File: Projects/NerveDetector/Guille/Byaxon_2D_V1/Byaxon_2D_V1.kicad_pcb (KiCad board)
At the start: 2 copper layers, 120.3 x 90 mm, 77 parts, among them U1 TL074

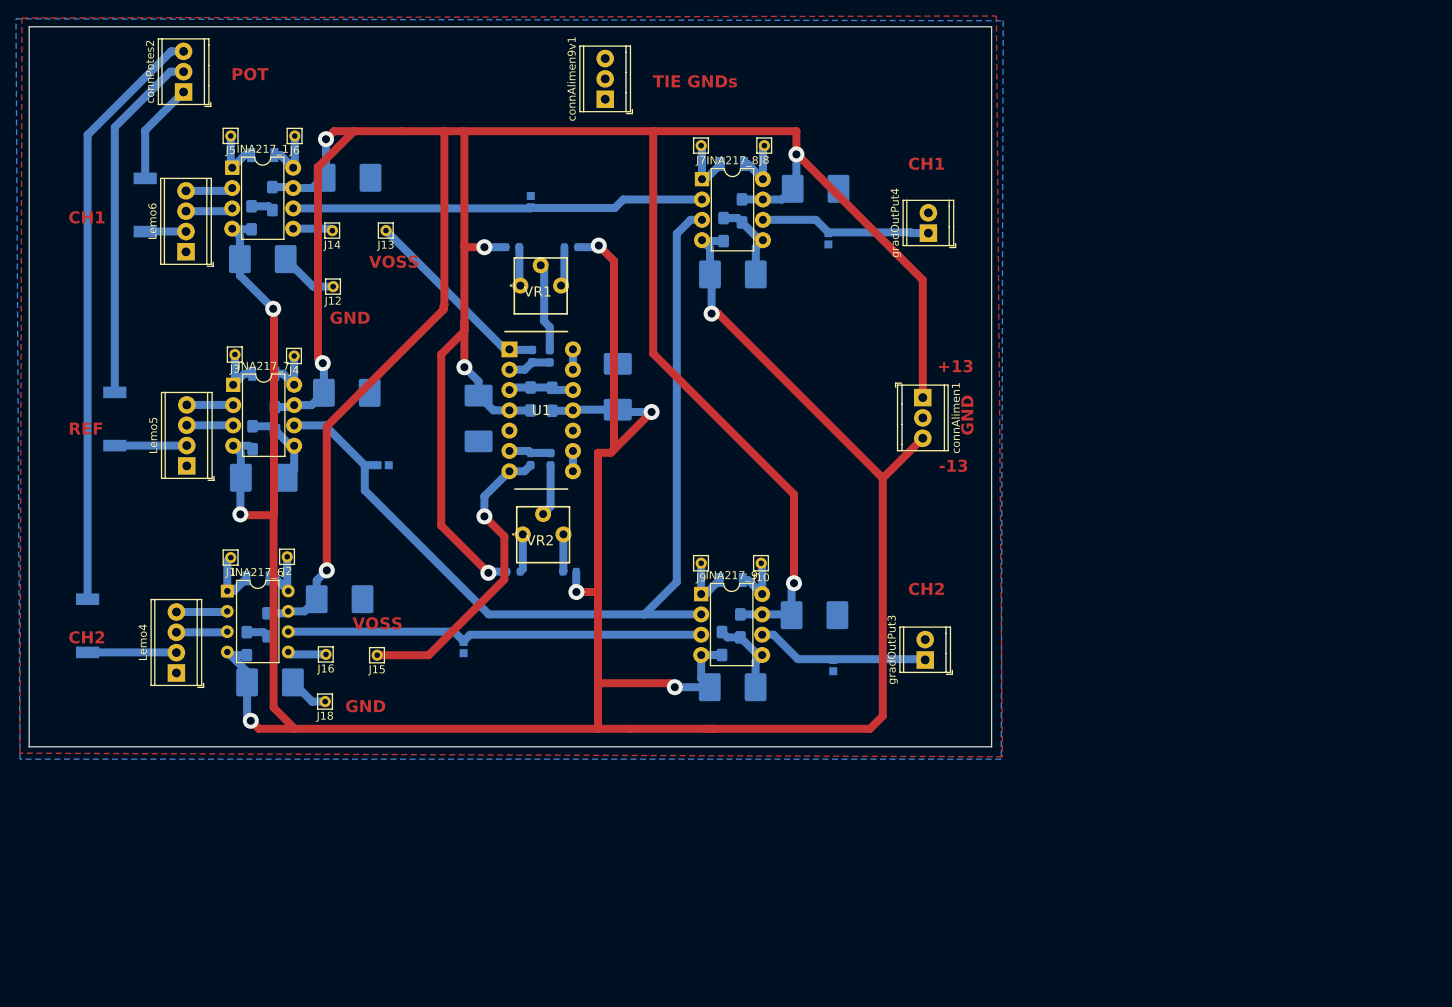
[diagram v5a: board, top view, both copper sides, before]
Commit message: Added link to projects github on the PCB
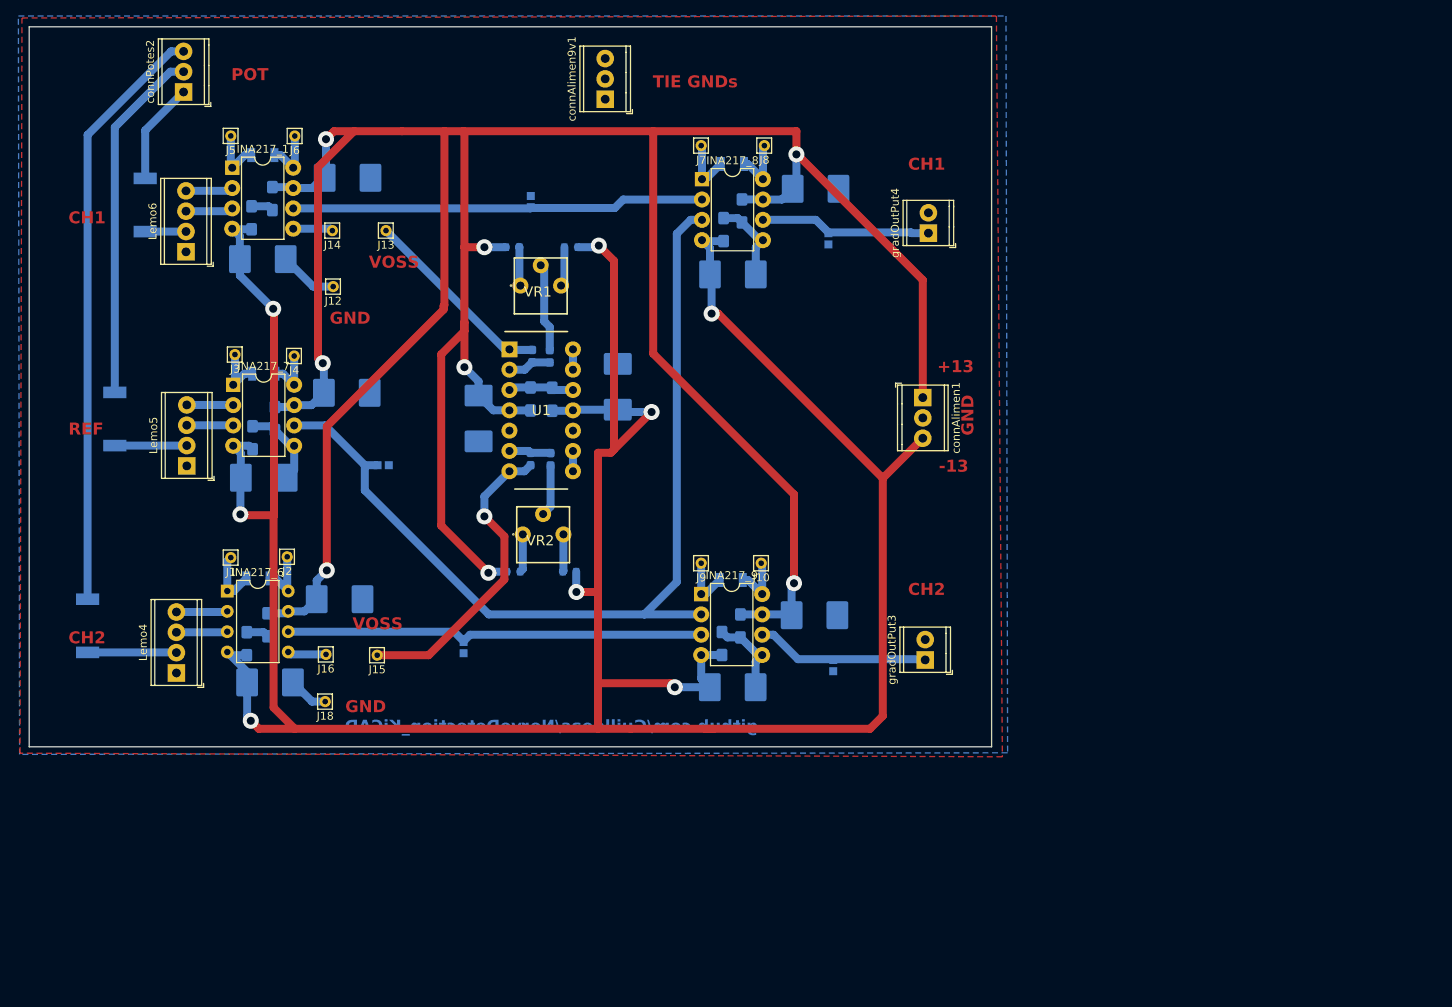
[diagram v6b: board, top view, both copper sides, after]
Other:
- board text added: "github.com/Guilldeas/NerveDetection_KiCAD"
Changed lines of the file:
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@@
     (effects (font (size 1.5 1.5) (thickness 0.3) bold) (justify left bottom))
+  )
+  (gr_text "github.com/Guilldeas/NerveDetection_KiCAD" (at 123.6 126.55) (layer "B.Cu")
+    (effects (font (size 1.5 1.5) (thickness 0.3) bold) (justify left bottom mirror))
   )
   (segment (start 112.7 120.3) (end 113.2 120.8) (width 1) (layer "F.Cu") (net 1))
@@
     (polygon
       (pts
-        (xy 30.85 37.25)
-        (xy 154.25 37.5)
-        (xy 154 129.8)
-        (xy 31.35 129.8)
+        (xy 154.6 36.9)
+        (xy 154.8 129)
+        (xy 31.3 129.2)
+        (xy 31.15 36.9)
       )
     )

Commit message: Added mounting holes
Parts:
- added H1: MountingHole, MountingHole:MountingHole_3.2mm_M3, F.Cu at (91.2, 72.0)
- added H2: MountingHole, MountingHole:MountingHole_3.2mm_M3, F.Cu at (90.5, 151.9)
- added H3: MountingHole, MountingHole:MountingHole_3.2mm_M3, F.Cu at (202.1, 152.9)
- added H4: MountingHole_Pad, MountingHole:MountingHole_3.2mm_M3_DIN965_Pad, F.Cu at (200.9, 72.0)
- moved C2 60.7 mm to (159.6, 112.0)
- moved C22 60.7 mm to (172.8, 92.3)
- moved R16 60.7 mm to (140.3, 144.6)
- moved R28 60.7 mm to (151.1, 108.2)
- moved VR2 60.7 mm to (150.2, 134.0)
- moved C39 60.7 mm to (116.4, 88.5)
- moved INA217_6 60.7 mm to (110.8, 137.5)
- moved Lemo4 60.7 mm to (104.4, 147.7)
- moved C1 60.7 mm to (142.2, 115.9)
- moved C21 60.7 mm to (174.0, 97.9)
- moved C23 60.7 mm to (116.7, 115.9)
- moved C24 60.7 mm to (125.7, 112.7)
- moved C25 60.7 mm to (184.2, 140.5)
- moved C27 60.7 mm to (175.1, 90.0)
- moved C28 60.7 mm to (172.6, 144.1)
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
